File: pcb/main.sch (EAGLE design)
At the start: 1 part

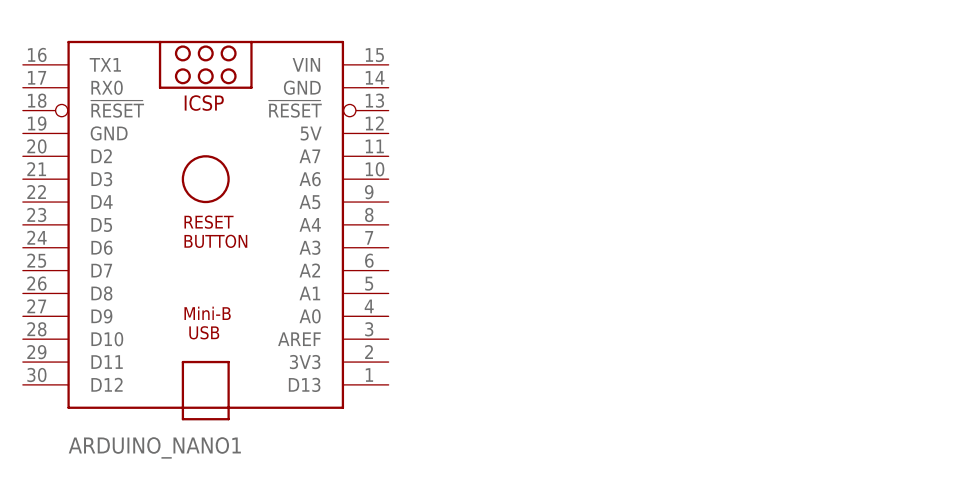
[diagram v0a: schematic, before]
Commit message: Added PCD8544 symbol and device
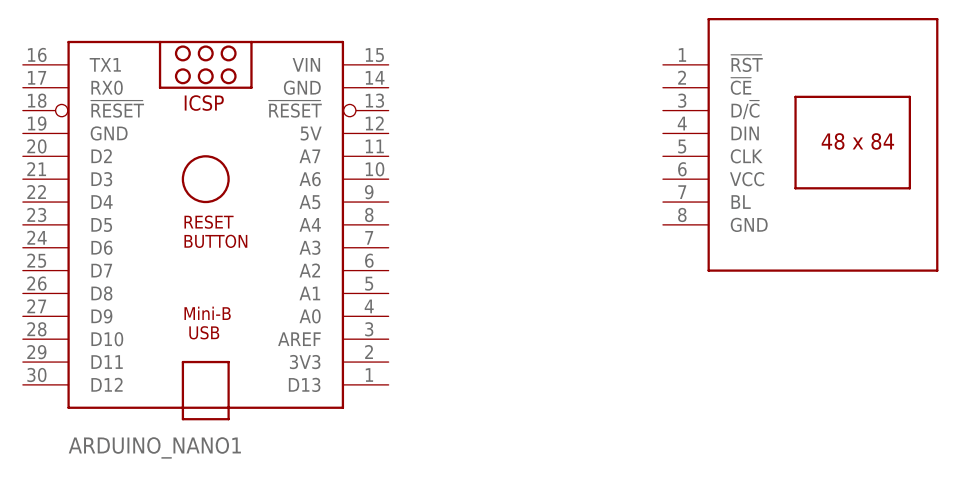
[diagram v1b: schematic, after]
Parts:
- added DISP1: PCD8544, PCD8544:PCD8544
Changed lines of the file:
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@@
 <setting verticaltext="up"/>
 </settings>
-<grid distance="0.1" unitdist="inch" unit="inch" style="lines" multiple="1" display="yes" altdistance="0.01" altunitdist="inch" altunit="inch"/>
+<grid distance="0.1" unitdist="inch" unit="inch" style="lines" multiple="1" display="no" altdistance="0.01" altunitdist="inch" altunit="inch"/>
 <layers>
 <layer number="1" name="Top" color="4" fill="1" visible="no" active="no"/>
@@
 <parts>
 <part name="ARDUINO_NANO1" library="ArduinoNanoV30" deviceset="ARDUINO_NANO" device=""/>
+<part name="DISP1" library="PCD8544" deviceset="PCD8544" device=""/>
 </parts>
 <sheets>
@@
 <attribute name="VALUE" x="30.48" y="50.8" size="1.778" layer="96"/>
 </instance>
+<instance part="DISP1" gate="G$1" x="114.3" y="86.36" smashed="yes"/>
 </instances>
 <busses>
